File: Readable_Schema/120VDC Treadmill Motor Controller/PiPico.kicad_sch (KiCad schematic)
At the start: 6 parts, among them J3 TB0011-350-08BE, J4 TB0011-350-08BE, J5 TB0011-350-08BE

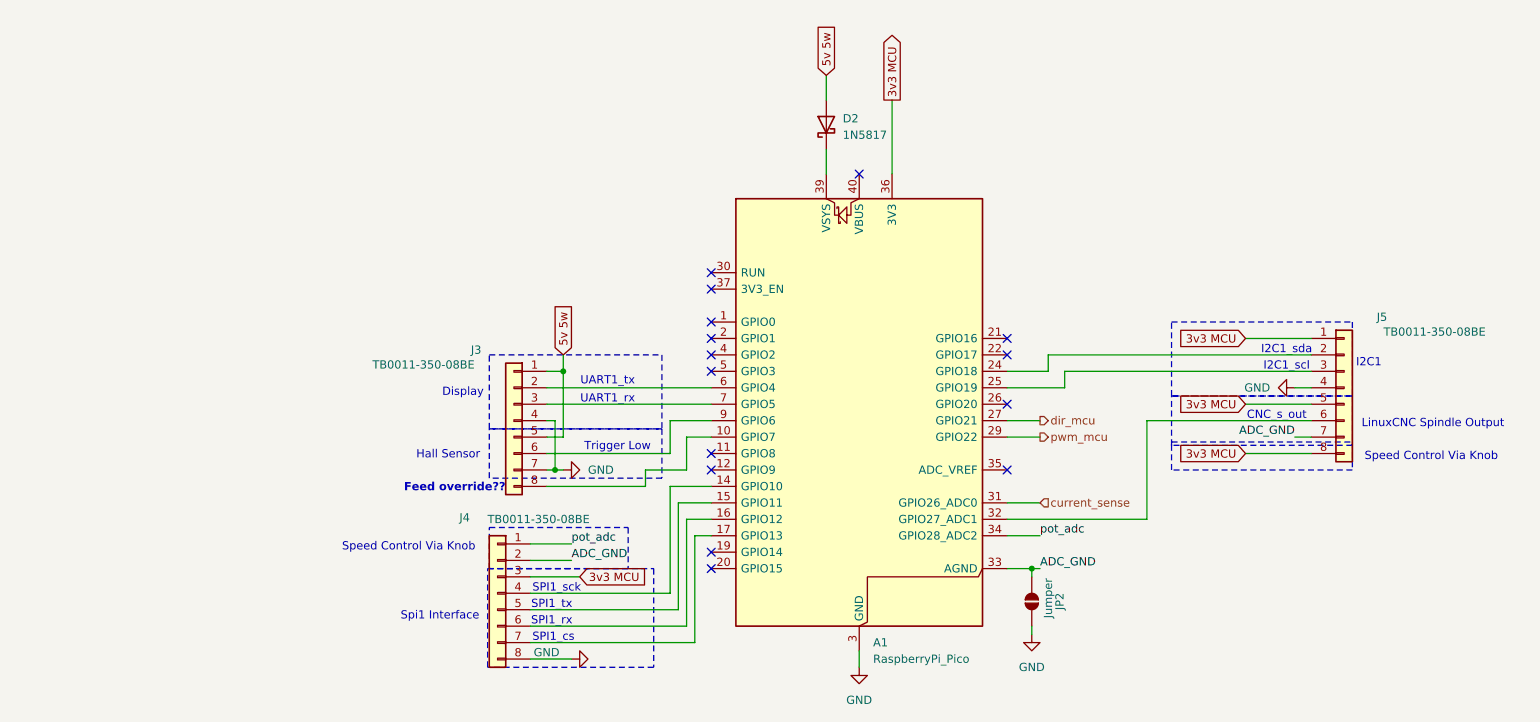
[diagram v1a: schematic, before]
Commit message: Changed ground naming and redid a bit of the pinouts between the pico and the h bridge -- need to fix the feedback loop to use a or gate for pwm_a and pwm_b to combine to one big reset
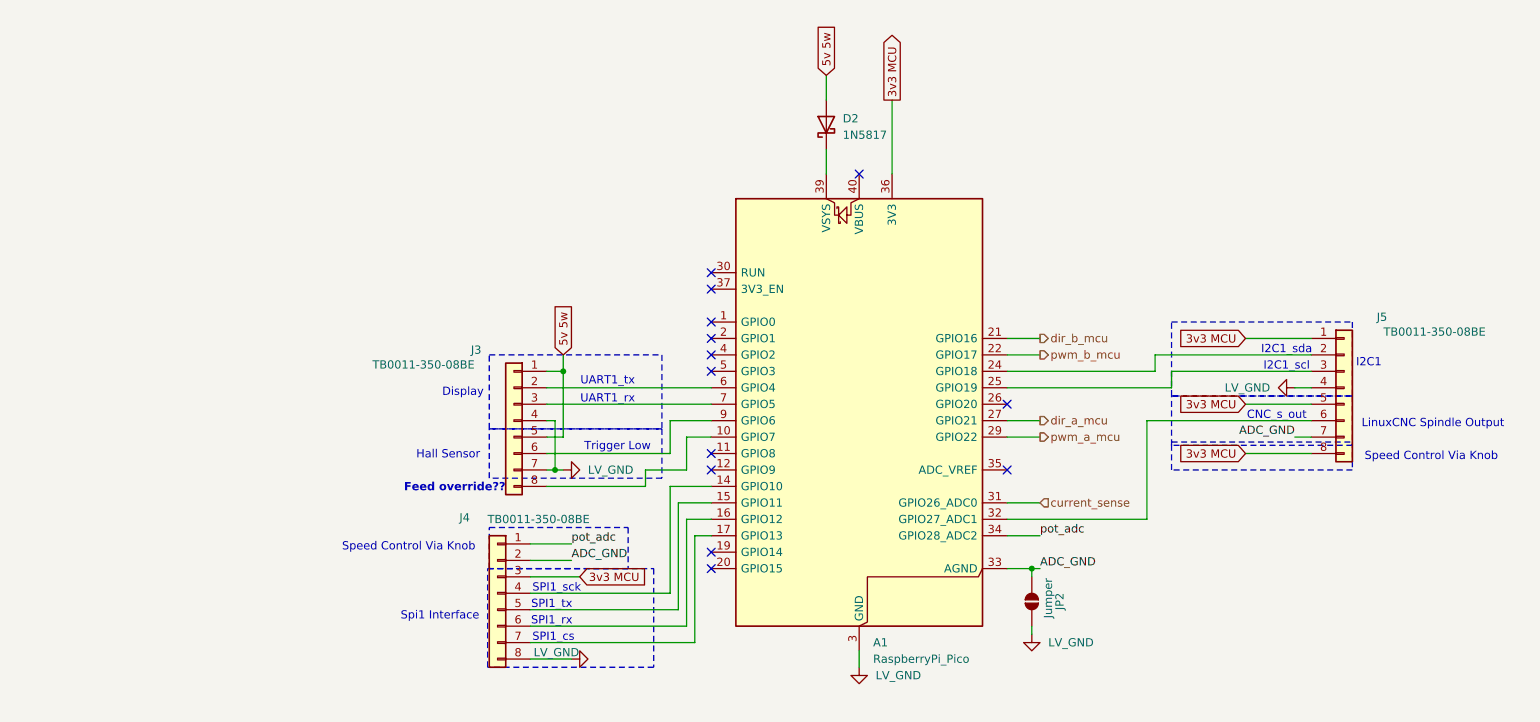
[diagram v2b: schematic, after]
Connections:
- net dir_b_mcu: now reaches A1.21 (GPIO16)
- net pwm_b_mcu: now reaches A1.22 (GPIO17)
- net GND renamed LV_GND
- net dir_mcu renamed dir_a_mcu
- net pwm_mcu renamed pwm_a_mcu
- no-connect marks 15 -> 13
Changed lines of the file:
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@@
-	)
-	(no_connect
-		(at 163.83 90.17)
 	)
 	(no_connect
@@
 	)
 	(no_connect
-		(at 163.83 87.63)
-	)
-	(no_connect
 		(at 163.83 97.79)
 	)
@@
 	(wire
 		(pts
-			(xy 172.72 92.71) (xy 210.82 92.71)
+			(xy 189.23 92.71) (xy 210.82 92.71)
 		)
 		(stroke
@@
 	(wire
 		(pts
-			(xy 170.18 92.71) (xy 170.18 90.17)
+			(xy 186.69 92.71) (xy 186.69 90.17)
 		)
 		(stroke
@@
 	(wire
 		(pts
-			(xy 172.72 95.25) (xy 172.72 92.71)
+			(xy 189.23 95.25) (xy 189.23 92.71)
+		)
+		(stroke
+			(width 0)
+			(type default)
+		)
+	)
+	(wire
+		(pts
+			(xy 163.83 87.63) (xy 168.91 87.63)
 		)
 		(stroke
@@
 	(wire
 		(pts
+			(xy 163.83 90.17) (xy 168.91 90.17)
+		)
+		(stroke
+			(width 0)
+			(type default)
+		)
+	)
+	(wire
+		(pts
 			(xy 208.28 102.87) (xy 210.82 102.87)
 		)
@@
 	(wire
 		(pts
-			(xy 163.83 95.25) (xy 172.72 95.25)
+			(xy 163.83 95.25) (xy 189.23 95.25)
 		)
 		(stroke
@@
 	(wire
 		(pts
-			(xy 170.18 90.17) (xy 210.82 90.17)
-		)
-		(stroke
-			(width 0)
-			(type default)
-		)
-	)
-	(wire
-		(pts
-			(xy 163.83 92.71) (xy 170.18 92.71)
+			(xy 186.69 90.17) (xy 210.82 90.17)
+		)
+		(stroke
+			(width 0)
+			(type default)
+		)
+	)
+	(wire
+		(pts
+			(xy 163.83 92.71) (xy 186.69 92.71)
 		)
 		(stroke
@@
 		)
 	)
-	(hierarchical_label "pwm_mcu"
+	(hierarchical_label "pwm_a_mcu"
 		(shape output)
 		(at 168.91 102.87 0)
@@
 		)
 	)
-	(hierarchical_label "dir_mcu"
+	(hierarchical_label "dir_b_mcu"
+		(shape output)
+		(at 168.91 87.63 0)
+		(effects
+			(font
+				(size 1.27 1.27)
+			)
+			(justify left)
+		)
+	)
+	(hierarchical_label "dir_a_mcu"
 		(shape output)
 		(at 168.91 100.33 0)
+		(effects
+			(font
+				(size 1.27 1.27)
+			)
+			(justify left)
+		)
+	)
+	(hierarchical_label "pwm_b_mcu"
+		(shape output)
+		(at 168.91 90.17 0)
 		(effects
 			(font
@@
 			)
 		)
-		(property "Value" "GND"
-			(at 140.97 143.51 0)
-			(effects
-				(font
-					(size 1.27 1.27)
-				)
+		(property "Value" "LV_GND"
+			(at 143.51 139.6999 0)
+			(effects
+				(font
+					(size 1.27 1.27)
+				)
+				(justify left)
 			)
 		)
@@
 			)
 		)
-		(property "Value" "GND"
+		(property "Value" "LV_GND"
 			(at 99.06 107.9499 90)
 			(effects
@@
 			)
 		)
-		(property "Value" "GND"
+		(property "Value" "LV_GND"
 			(at 204.47 95.2499 90)
 			(effects
@@
 			)
 		)
-		(property "Value" "GND"
+		(property "Value" "LV_GND"
 			(at 90.678 136.144 90)
 			(effects
@@
 			)
 		)
-		(property "Value" "GND"
-			(at 167.64 138.43 0)
-			(effects
-				(font
-					(size 1.27 1.27)
-				)
-			)
-		)
+		(property "Value" "LV_GND"
+			(at 170.18 134.6199 0)
+			(effects
+				(font
+					(size 1.27 1.27)
+				)
+				(justify left)
+			)
+		)

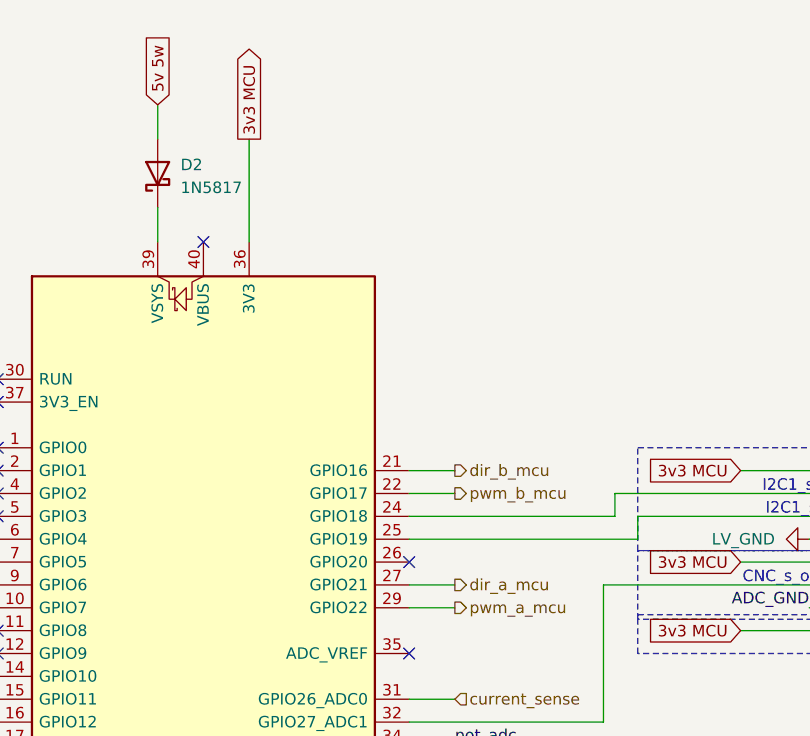
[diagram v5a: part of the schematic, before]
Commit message: -Changed the precharge circuit gate driver to the TP5I3 --This gate driver provides its own 10v isolated PS, which saves a lot of room
-changed the schottky for the pi pico to a smd equivalent.
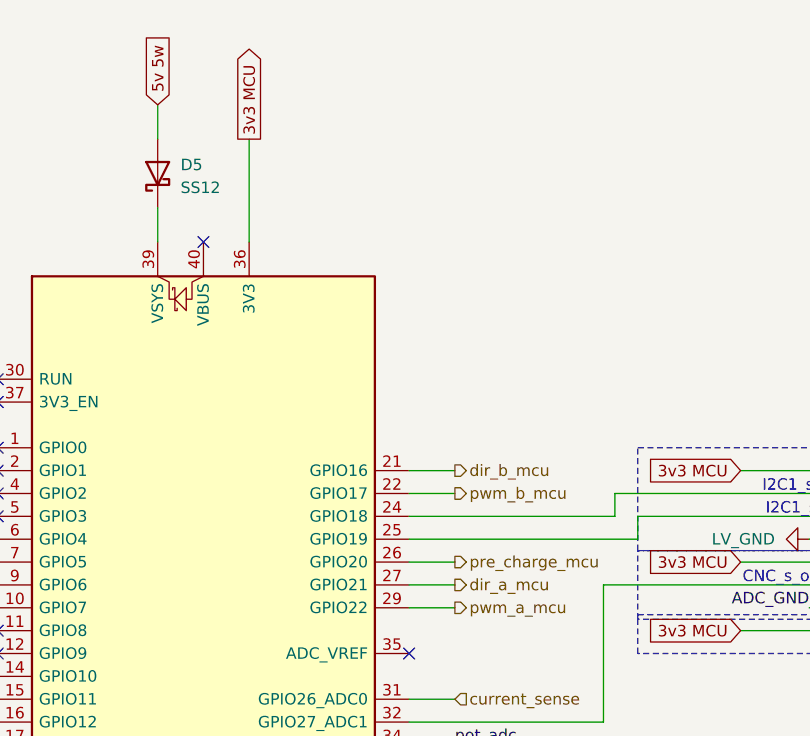
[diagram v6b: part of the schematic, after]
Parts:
- removed D2: 1N5817, Diode_THT:D_DO-41_SOD81_P10.16mm_Horizontal, symbol Diode:1N5817
- added D5: SS12, Diode_SMD:D_SMA, symbol Diode:SS12
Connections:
- net 5v 5w: now also D5.2 (A)
- net pre_charge_mcu: now reaches A1.26 (GPIO20)
- net at A1.39 (VSYS): now also D5.1 (K)
- no-connect marks 13 -> 12
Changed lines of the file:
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@@
-	)
-	(no_connect
-		(at 163.83 97.79)
 	)
 	(no_connect
@@
 		(pts
 			(xy 186.69 92.71) (xy 186.69 90.17)
+		)
+		(stroke
+			(width 0)
+			(type default)
+		)
+	)
+	(wire
+		(pts
+			(xy 163.83 97.79) (xy 168.91 97.79)
 		)
 		(stroke
@@
 		)
 	)
+	(hierarchical_label "pre_charge_mcu"
+		(shape output)
+		(at 168.91 97.79 0)
+		(effects
+			(font
+				(size 1.27 1.27)
+			)
+			(justify left)
+		)
+	)
 	(hierarchical_label "dir_a_mcu"
 		(shape output)
@@
 			)
 			(justify left)
+		)
+	)
+	(symbol
+		(lib_id "Diode:SS12")
+		(at 135.89 54.61 90)
+		(unit 1)
+		(exclude_from_sim no)
+		(in_bom yes)
+		(on_board yes)
+		(dnp no)
+		(fields_autoplaced yes)
+		(property "Reference" "D5"
+			(at 138.43 53.6574 90)
+			(effects
+				(font
+					(size 1.27 1.27)
+				)
+				(justify right)
+			)
+		)
+		(property "Value" "SS12"
+			(at 138.43 56.1974 90)
+			(effects
+				(font
+					(size 1.27 1.27)
+				)
+				(justify right)
+			)
+		)
+		(property "Footprint" "Diode_SMD:D_SMA"
+			(at 140.335 54.61 0)
+			(effects
+				(font
+					(size 1.27 1.27)
+				)
+				(hide yes)
+			)
+		)
+		(property "Datasheet" "https://www.vishay.com/docs/88746/ss12.pdf"
+			(at 135.89 54.61 0)
+			(effects
+				(font
+					(size 1.27 1.27)
+				)
+				(hide yes)
+			)
+		)
+		(property "Description" "20V 1A Schottky Diode, SMA"
+			(at 135.89 54.61 0)
+			(effects
+				(font
+					(size 1.27 1.27)
+				)
+				(hide yes)
+			)
+		)
+		(pin "1"
+		)
+		(pin "2"
+		)
+		(instances
+			(project ""
+				(path "/319bc5c0-2dd5-4df3-a34b-9170833ebccd/dc45a2ff-df18-49a4-81ff-80d10381c9e9"
+					(reference "D5")
+					(unit 1)
+				)
+			)
 		)
 	)
@@
 					(unit 1)
 				)
-			)
-		)
-	)
-	(symbol
-		(lib_id "Diode:1N5817")
-		(at 135.89 54.61 90)
-		(unit 1)
-		(exclude_from_sim no)
-		(in_bom yes)
-		(on_board yes)
-		(dnp no)
-		(fields_autoplaced yes)
-		(property "Reference" "D2"
-			(at 138.43 53.6574 90)
-			(effects
-				(font
-					(size 1.27 1.27)
-				)
-				(justify right)
-			)
-		)
-		(property "Value" "1N5817"
-			(at 138.43 56.1974 90)
-			(effects
-				(font
-					(size 1.27 1.27)
-				)
-				(justify right)
-			)
-		)
-		(property "Footprint" "Diode_THT:D_DO-41_SOD81_P10.16mm_Horizontal"
-			(at 140.335 54.61 0)
-			(effects
-				(font
-					(size 1.27 1.27)
-				)
-				(hide yes)
-			)
-		)
-		(property "Datasheet" "http://www.vishay.com/docs/88525/1n5817.pdf"
-			(at 135.89 54.61 0)
-			(effects
-				(font
-					(size 1.27 1.27)
-				)
-				(hide yes)
-			)
-		)
-		(property "Description" "20V 1A Schottky Barrier Rectifier Diode, DO-41"
-			(at 135.89 54.61 0)
-			(effects
-				(font
-					(size 1.27 1.27)
-				)
-				(hide yes)
-			)
-		)
-		(pin "1"
-		)
-		(pin "2"
-		)
-		(instances
-			(project ""
-				(path "/319bc5c0-2dd5-4df3-a34b-9170833ebccd/dc45a2ff-df18-49a4-81ff-80d10381c9e9"
-					(reference "D2")
-					(unit 1)
-				)

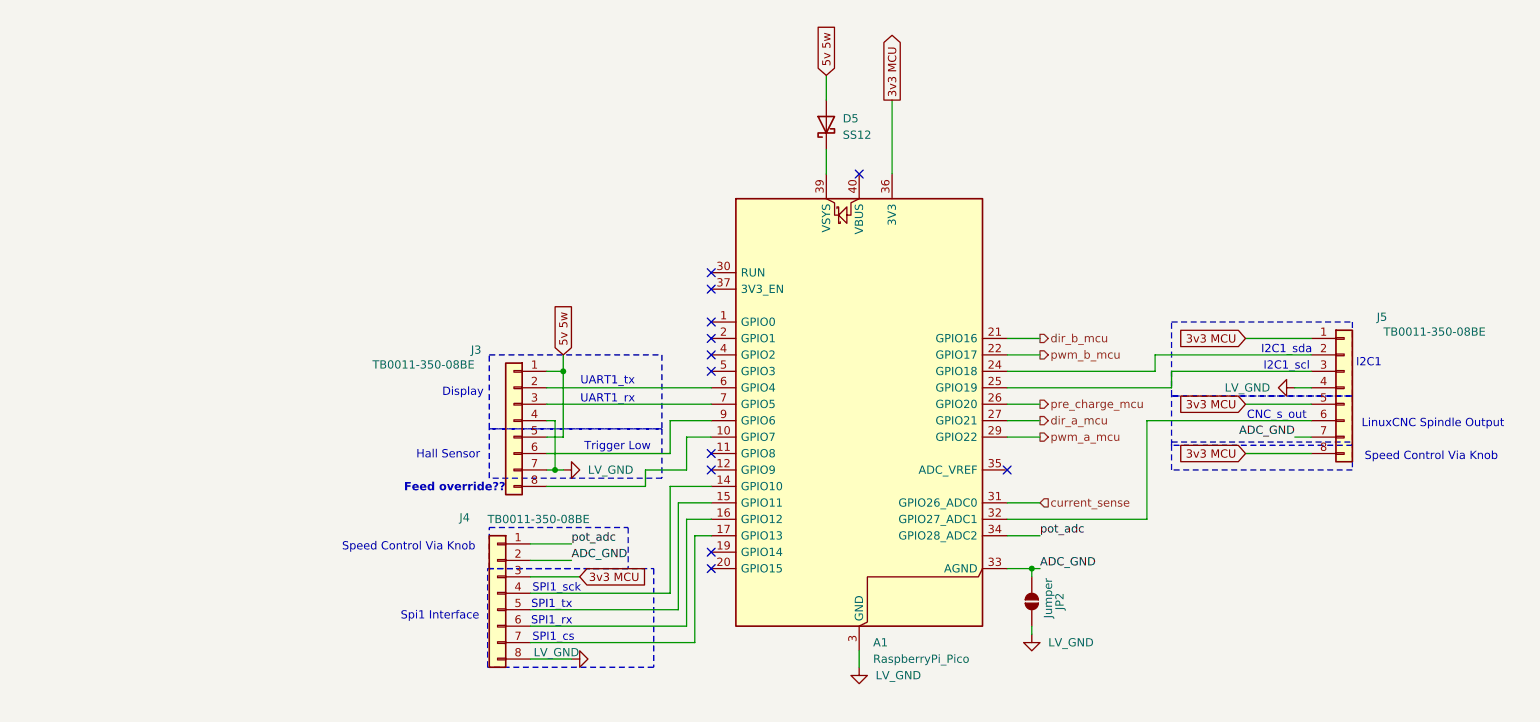
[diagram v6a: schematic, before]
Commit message: -Added voltage sense
-Need to add some kind of LED to tell that the board is HOT

-Need to work with ross to understand the DNMOS setup
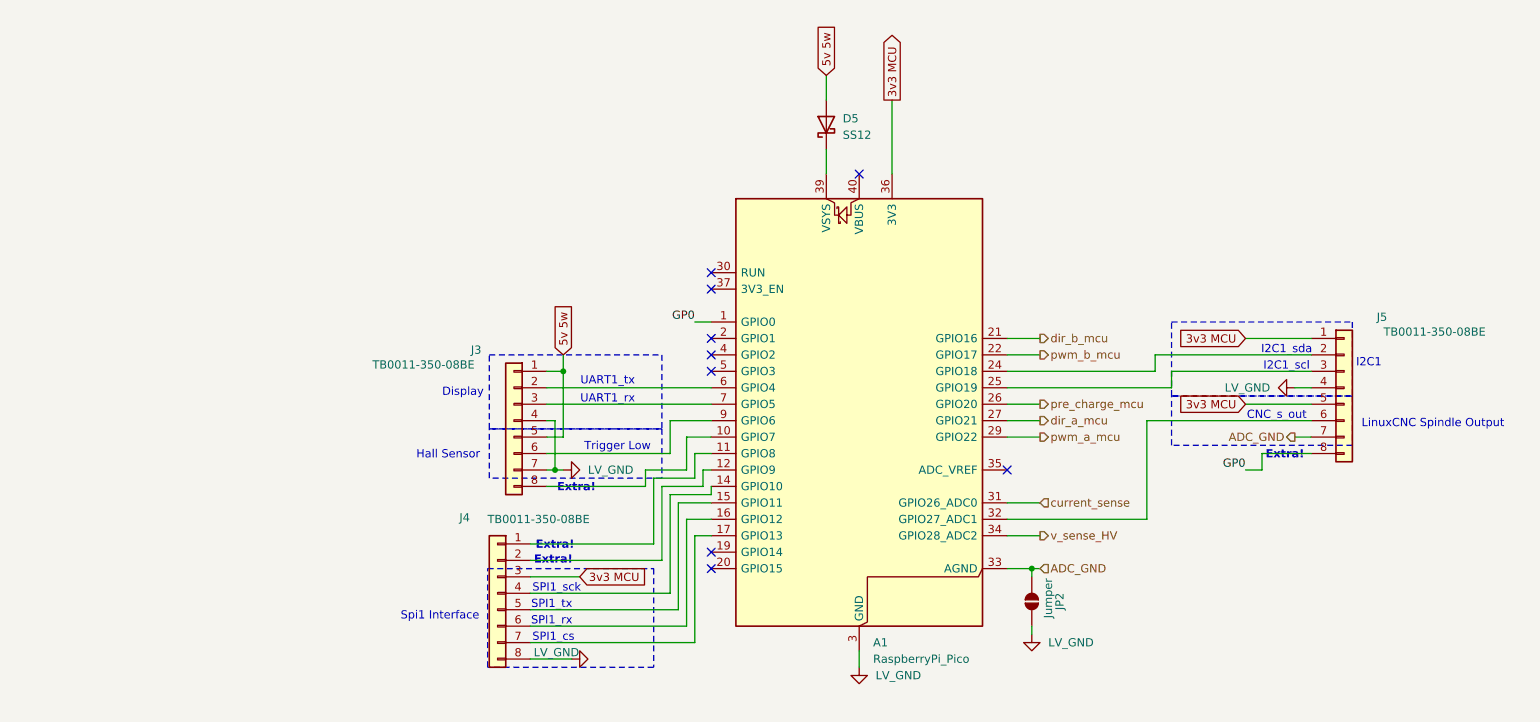
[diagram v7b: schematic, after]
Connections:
- net 3v3 MCU: no longer J5.8 (Pin_8)
- net ADC_GND: no longer J4.2 (Pin_2)
- net GP0: now reaches A1.1 (GPIO0)
- net GP0: now also J5.8 (Pin_8)
- net at A1.11 (GPIO8): now also J4.1 (Pin_1)
- net at A1.12 (GPIO9): now also J4.2 (Pin_2)
- net pot_adc renamed v_sense_HV
- net v_sense_HV: no longer J4.1 (Pin_1)
- no-connect marks 12 -> 9
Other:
- note added: "Extra!"
- note removed: "Feed override??"
- note removed: "Speed Control Via Knob"
